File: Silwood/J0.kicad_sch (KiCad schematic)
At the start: 0 parts

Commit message: update
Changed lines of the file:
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@@
+		)
+	)
+	(global_label "D"
+		(shape input)
+		(at 132.715 61.595 0)
+		(fields_autoplaced yes)
+		(effects
+			(font
+				(size 1.27 1.27)
+			)
+			(justify left)
+		)
+		(property "Intersheetrefs" "${INTERSHEET_REFS}"
+			(at 136.316 61.595 0)
+			(effects
+				(font
+					(size 1.27 1.27)
+				)
+				(justify left)
+				(hide yes)
+			)
 		)
 	)

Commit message: j0
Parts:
- added PT72, PT73: ~, symbol PID_symbols:Pressure_Transducer
- added U5, U6, U7, U8: ~, symbol PID_symbols:stop
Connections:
- new net 1-2: U5., U8.
- new net 1-4: PT72., U8.
- new net 3-8: U5.
- new net ATM: U7.
- new net N2O Bay/Ox_External_Vent: U7.
- new net Pressure Panel1/N2_LP: PT73., U6.
- new net Tube: U6.
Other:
- sheet N2O Bay ports: added Ox_External_Vent; removed none
- note added: "1 INCH"
- note added: "1-2 INCH"
- note added: "1-4 INCH"
- note added: "1-8 INCH"
- note added: "3-4 INCH"
- note added: "3-8 INCH"
- note added: "Container Wall"
- note added: "Direct Connection"
- note added: "Low Pressure Pneumatics"
- note added: "Torch Igniter High Pressure Line"
- note added: "Torch Igniter Pneumatics Line"

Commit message: more silwood stuff
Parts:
- removed PT72: ~, symbol PID_symbols:Pressure_Transducer
- removed U8: ~, symbol PID_symbols:stop
- added Engine1: ~, symbol PID_symbols:Engine
- added Hose1, Hose2: ~, symbol PID_symbols:Hose
- added PT1, PT3, PT4: ~, symbol PID_symbols:Pressure_Transducer
- added Pmatic_B_Valve1: ~, symbol PID_symbols:Pneumatic_Rotary_Ball_Valve
- added TC1, TC2: ~, symbol PID_symbols:Thermocouple
- added U10, U11, U13, U14, U6, U7, U9: ~, symbol PID_symbols:stop
- renumbered PT73 to PT2, U5 to U12, U7 to U5, U6 to U8
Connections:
- net 1: now also Engine1., Hose1., U7.
- net 1-2: now also Pmatic_B_Valve1., U13., U9.
- net 1-4: now also PT1., PT3., PT4., TC1., TC2., U10., U7., U9.
- net 3-4: now also Engine1., Hose2., U10.
- net ATM: now also U13., U14.
- net Tube: now also Pmatic_B_Valve1.
- new net Fuel Bay/Fuel_Delivery: Hose2., U11.
- new net Fuel Bay/Fuel_External_Vent: U14.
- new net Fuel Bay/N2_Purge_Fuel: U11.
- new net N2O Bay/N20_Delivery: Hose1., U6.
- new net N2O Bay/N2_Purge_Ox: U6.
- no-connect marks 0 -> 3
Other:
- sheet Fuel Bay ports: added Fuel_Delivery, Fuel_External_Vent, N2_HP, N2_LP, N2_Purge_Fuel; removed none
- sheet N2O Bay ports: added N20_Delivery, N2_Purge_Ox; removed none
- moved on the sheet: PT2

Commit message: bit more
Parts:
- added Pmatic_B_Valve10: ~, symbol PID_symbols:Pneumatic_Rotary_Ball_Valve
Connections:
- net 1-2: now also Pmatic_B_Valve10.
- net Tube: now also Pmatic_B_Valve10.
- new net N2 Bottles/N2_HP: Pmatic_B_Valve10.
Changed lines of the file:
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@@
+	)
+	(junction
+		(at 135.255 79.375)
+		(diameter 0)
+		(color 0 0 0 0)
 	)
 	(junction
@@
 	(wire
 		(pts
+			(xy 135.255 79.375) (xy 140.97 79.375)
+		)
+		(stroke
+			(width 0)
+			(type default)
+		)
+	)
+	(wire
+		(pts
 			(xy 105.41 154.94) (xy 105.41 161.29)
 		)
@@
 	(wire
 		(pts
+			(xy 146.685 61.595) (xy 135.255 61.595)
+		)
+		(stroke
+			(width 0)
+			(type default)
+		)
+	)
+	(wire
+		(pts
 			(xy 129.54 147.32) (xy 117.475 147.32)
 		)
@@
 	(wire
 		(pts
+			(xy 135.255 61.595) (xy 135.255 79.375)
+		)
+		(stroke
+			(width 0)
+			(type default)
+		)
+	)
+	(wire
+		(pts
 			(xy 46.355 113.665) (xy 62.865 113.665)
 		)
@@
 	(wire
 		(pts
+			(xy 153.035 55.245) (xy 160.02 55.245)
+		)
+		(stroke
+			(width 0)
+			(type default)
+		)
+	)
+	(wire
+		(pts
 			(xy 120.65 26.67) (xy 139.065 26.67)
 		)
@@
 	(wire
 		(pts
-			(xy 139.065 55.245) (xy 160.02 55.245)
+			(xy 139.065 55.245) (xy 140.335 55.245)
 		)
 		(stroke
@@
 	(wire
 		(pts
-			(xy 109.22 79.375) (xy 140.97 79.375)
+			(xy 109.22 79.375) (xy 135.255 79.375)
 		)
 		(stroke
@@
 					(unit 1)
 				)
+			)
+		)
+	)
+	(symbol
+		(lib_name "Pneumatic_Rotary_Ball_Valve_1")
+		(lib_id "PID_symbols:Pneumatic_Rotary_Ball_Valve")
+		(at 146.685 55.245 180)
+		(unit 1)
+		(exclude_from_sim no)
+		(in_bom yes)
+		(on_board yes)
+		(dnp no)
+		(property "Reference" "Pmatic_B_Valve10"
+			(at 126.365 50.165 0)
+			(effects
+				(font
+					(size 1.27 1.27)
+				)
+			)
+		)
+		(property "Value" "~"
+			(at 146.685 55.245 0)
+			(effects
+				(font
+					(size 1.27 1.27)
+				)
+				(hide yes)
+			)
+		)
+		(property "Footprint" ""
+			(at 146.685 55.245 0)
+			(effects
+				(font
+					(size 1.27 1.27)
+				)
+				(hide yes)
+			)
+		)
+		(property "Datasheet" ""
+			(at 146.685 55.245 0)
+			(effects
+				(font
+					(size 1.27 1.27)
+				)
+				(hide yes)
+			)
+		)
+		(property "Description" ""
+			(at 146.685 55.245 0)
+			(effects
+				(font
+					(size 1.27 1.27)
+				)
+			)
+		)
+		(pin ""
+		)
+		(pin ""
+		)
+		(pin ""
+		)
+		(pin ""
+		)
+		(instances
+			(project ""
+				(path "/045f1f05-3134-4b6d-91b6-463031104f1e/a0b6300e-76e9-4a18-afd6-e2d656b0d8f9/d375e00a-1ce3-4f93-9279-82acf09c7292"
+					(reference "Pmatic_B_Valve10")
+					(unit 1)
+				)

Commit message: silwood upgrade
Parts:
- removed U9: ~, symbol PID_symbols:stop
- added PT83, PT84, PT85: ~, symbol PID_symbols:Pressure_Transducer
- added QD24, QD25: ~, symbol PID_symbols:Quick_Disconnect
- added U68: ~, symbol PID_symbols:Solid_Igniter
- added nC_Sol8, nC_Sol9: ~, symbol PID_symbols:Normally_Closed_Solenoid
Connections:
- net 1-2: no longer U12.
- net 1-4: no longer PT4.
- net N2 Bottles/N2_HP: now also PT4., U12.
- new net: PT84., QD25., nC_Sol9.
- new net: PT85., QD24., nC_Sol8.
- new net: PT83., U68., nC_Sol8., nC_Sol9.
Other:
- moved on the sheet: Pmatic_B_Valve10

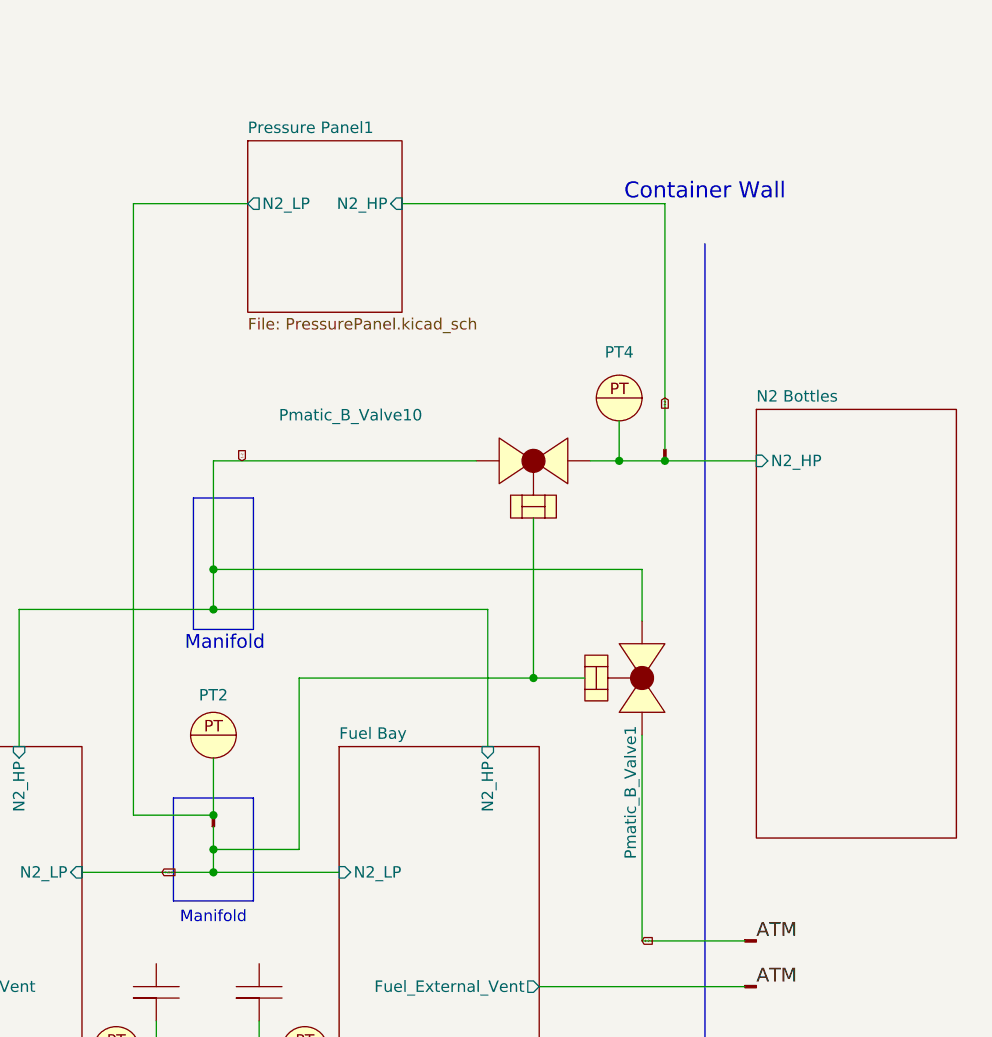
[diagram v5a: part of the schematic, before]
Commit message: fixed netclass definitions
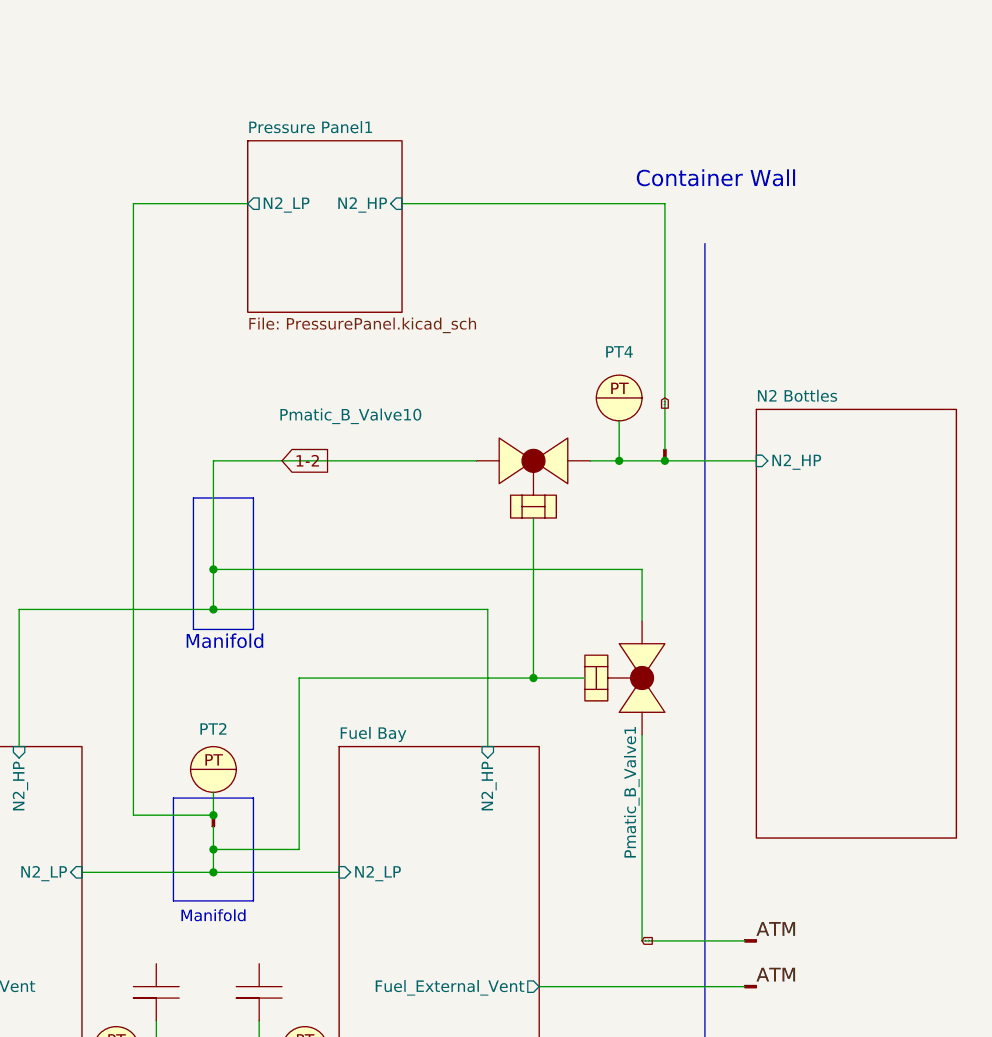
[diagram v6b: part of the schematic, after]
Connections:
- net Tube: no longer Pmatic_B_Valve1., Pmatic_B_Valve10., U8.
- net at QD25.: now also PT84., nC_Sol9.
- net at QD24.: now also PT85., nC_Sol8.
- net Fuel Bay/N2_LP: now reaches Pmatic_B_Valve1.
- net Fuel Bay/N2_LP: now also Pmatic_B_Valve10., U8.
- now unconnected: PT84., PT85.
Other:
- moved on the sheet: PT2
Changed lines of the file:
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@@
 	(text "Container Wall"
 		(exclude_from_sim no)
-		(at 154.305 25.4 0)
+		(at 155.575 24.13 0)
 		(effects
 			(font
@@
 	(wire
 		(pts
-			(xy 99.695 88.265) (xy 99.695 94.615)
+			(xy 99.695 92.075) (xy 99.695 94.615)
 		)
 		(stroke
@@
 		)
 	)
-	(global_label "Tube"
+	(global_label "1-2"
 		(shape input)
-		(at 93.98 100.965 0)
-		(fields_autoplaced yes)
-		(effects
-			(font
-				(size 0.254 0.254)
+		(at 107.315 55.245 0)
+		(fields_autoplaced yes)
+		(effects
+			(font
+				(size 1.27 1.27)
 			)
 			(justify left)
 		)
 		(property "Intersheetrefs" "${INTERSHEET_REFS}"
-			(at 95.3174 100.965 0)
+			(at 113.6374 55.245 0)
 			(effects
 				(font
@@
 		(property "Intersheetrefs" "${INTERSHEET_REFS}"
 			(at 241.9074 24.765 0)
-			(effects
-				(font
-					(size 1.27 1.27)
-				)
-				(justify left)
-				(hide yes)
-			)
-		)
-	)
-	(global_label "1-2"
-		(shape input)
-		(at 102.87 55.245 90)
-		(fields_autoplaced yes)
-		(effects
-			(font
-				(size 0.254 0.254)
-			)
-			(justify left)
-		)
-		(property "Intersheetrefs" "${INTERSHEET_REFS}"
-			(at 102.87 53.9801 90)
 			(effects
 				(font
@@
 	(symbol
 		(lib_id "PID_symbols:Pressure_Transducer")
-		(at 99.695 85.725 0)
+		(at 99.695 89.535 0)
 		(unit 1)
 		(exclude_from_sim no)
@@
 		(fields_autoplaced yes)
 		(property "Reference" "PT2"
-			(at 99.695 81.28 0)
+			(at 99.695 85.09 0)
 			(effects
 				(font
@@
 		)
 		(property "Value" "~"
-			(at 99.695 86.995 0)
+			(at 99.695 90.805 0)
 			(effects
 				(font
@@
 		)
 		(property "Footprint" ""
-			(at 99.695 85.725 0)
+			(at 99.695 89.535 0)
 			(effects
 				(font
@@
 		)
 		(property "Datasheet" ""
-			(at 99.695 85.725 0)
+			(at 99.695 89.535 0)
 			(effects
 				(font
@@
 		)
 		(property "Description" ""
-			(at 99.695 85.725 0)
-			(effects
-				(font
+			(at 99.695 89.535 0)
+			(effects
+				(font

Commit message: big silwood update
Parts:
- removed PT84, PT85: ~, symbol PID_symbols:Pressure_Transducer
- removed QD25: ~, symbol PID_symbols:Quick_Disconnect
- removed U68: ~, symbol PID_symbols:Solid_Igniter
- removed nC_Sol9: ~, symbol PID_symbols:Normally_Closed_Solenoid
- added BV7: ~, symbol PID_symbols:Ball_Valve
- added Burst_Disc18: ~, symbol PID_symbols:Burst_Disc
- added CF3: ~, symbol PID_symbols:Coriolis_Flow
- added CV10: ~, symbol PID_symbols:Check_Valve
- added DP3: ~, symbol PID_symbols:DP_Sensor
- added Dome3: ~, symbol PID_symbols:Dome_Reg
- added Filter17: ~, symbol PID_symbols:Filter
- added MB_V2: ~, symbol PID_symbols:MBallValve
- added Manual_Pressure_Gauge21: ~, symbol PID_symbols:Manual_Pressure_Gauge
- added Pmatic_B_Valve11: ~, symbol PID_symbols:Pneumatic_Rotary_Ball_Valve
- added SPRV27, SPRV28: ~, symbol PID_symbols:SPRV
- added Servo_Reg17, Servo_Reg3: ~, symbol PID_symbols:Pressure_Regulator
- added TC9: ~, symbol PID_symbols:Thermocouple
- added U69: ~, symbol PID_symbols:stop
- added nO_Sol26: ~, symbol PID_symbols:Normally Open Solenoid
- Pmatic_B_Valve1: value ~ -> D2
- Pmatic_B_Valve10: value ~ -> D1
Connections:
- net 1-2: now also SPRV28.
- net N2 Bottles/N2_HP: now also SPRV28.
- net N2O Bay/Ox_External_Vent: now also U69.
- net at nC_Sol8.: no longer QD24.
- net at PT83.: no longer nC_Sol8.
- new net N20 BOTTLES/N2O_Vent: U69.
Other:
- sheet N20 BOTTLES ports: added N2O_Vent; removed none
- note added: "(4): Optional Numbering if multiple sensors in same local feed line Smaller number is upstream."
- note added: "1: Macro location of component KEY: O: Oxidiser panel F: Fuel panel N: Outer N2 System I: Igniter PP: Pressure Panel OB: Oxidiser outside bottles"
- note added: "2: Component Type KEY: Bv: Ball Valve (servo actuated) Mbv: Manual Ball Valve Mf: Massflow control Ball Valve Pn: Pneumatic Actuated Valves Sol: Solenoid Valves PT: Pressure Transducer Tc: Thermocouple Reg: Pressure Regulator CFM: Coriolis Flow Meter PG: Pressure Gauge Tk: Tank Prv: Pressure Relief Valve BD: Burst Disk DP: Differential Pressure Sensor"
- note added: "3: Local Location feed system of Component KEY: Ref: Dome reference pressure system M: Main run line V: Venting Line T: Tank Pressurisation Line N: Nitrogen High Pressure Source Line O: Oxidiser Source Line F: Fill Line D: Drain Line P: Purge Line LP: Low Pressure Impulse Air Line"
- note added: "Burst Disk"
- note added: "Check-Valve"
- note added: "Component Naming Scheme: 1_2_3(4)"
- note added: "Coriolis Flow Meter"
- note added: "Deployment Line 1: 'D1' Run Valves on N2 lines to tanks, and main lines."
- note added: "Deployment Line 2: 'D2' All venting valves."
- note added: "Differential Pressure Transducer"
- note added: "Dome-Loaded Regulator"
- note added: "Filter"
- note added: "Manual Ball Valve"
- note added: "Normally Closed Solenoid"
- note added: "Normally Open Solenoid"
- note added: "Pneumatic Actuated Valve, NO/NC (Normally Open/Closed)"
- note added: "Pressure Gauge"
- note added: "Pressure Regulator"
- note added: "Pressure Relief Valve"
- note added: "Pressure Transducer"
- note added: "Quick-Disconnect"
- note added: "Servo Ball Valve"
- note added: "Servo-Actuated Pressure Regulator"
- note added: "Thermocouple"
- moved on the sheet: PT1, PT3, TC1, TC2

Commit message: update
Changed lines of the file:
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@@
 	(paper "User" 381 210)
 	(rectangle
-		(start 97.4725 59.3725)
+		(start 96.5199 59.3725)
 		(end 104.1399 73.9775)
 		(stroke
